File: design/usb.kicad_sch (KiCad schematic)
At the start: 27 parts, among them J4 USB_B_Mini, SW1 RST, U7 SN74LVC1G11DCKR, U8 USBLC6-2SC6, U9 FT231XS

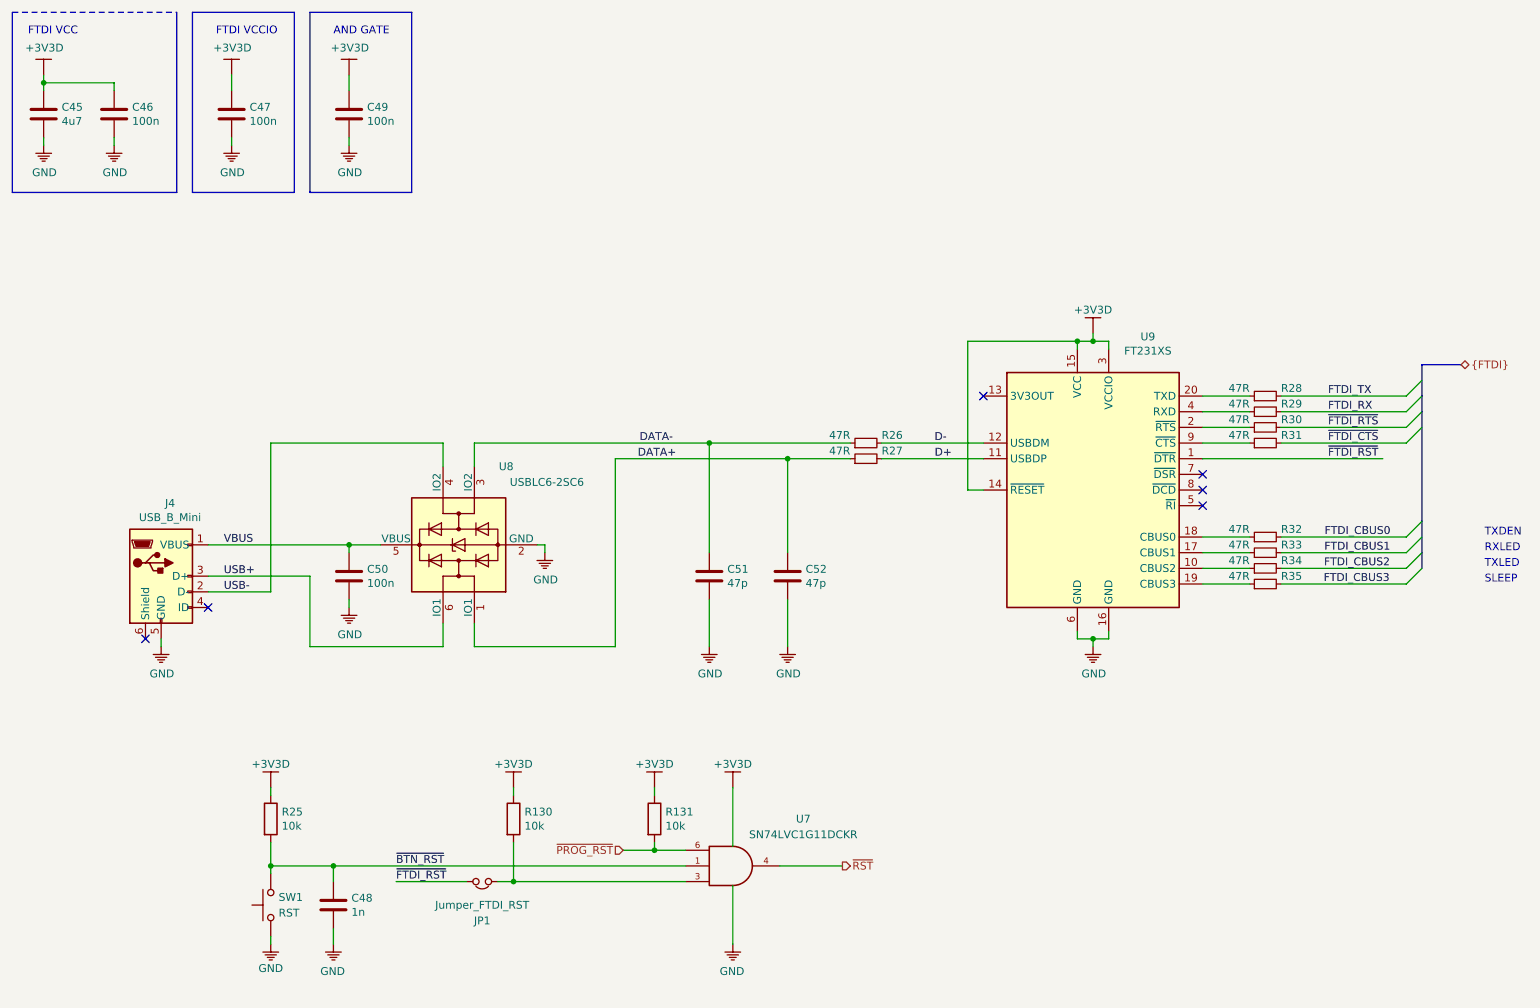
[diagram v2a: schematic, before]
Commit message: Added fiducials
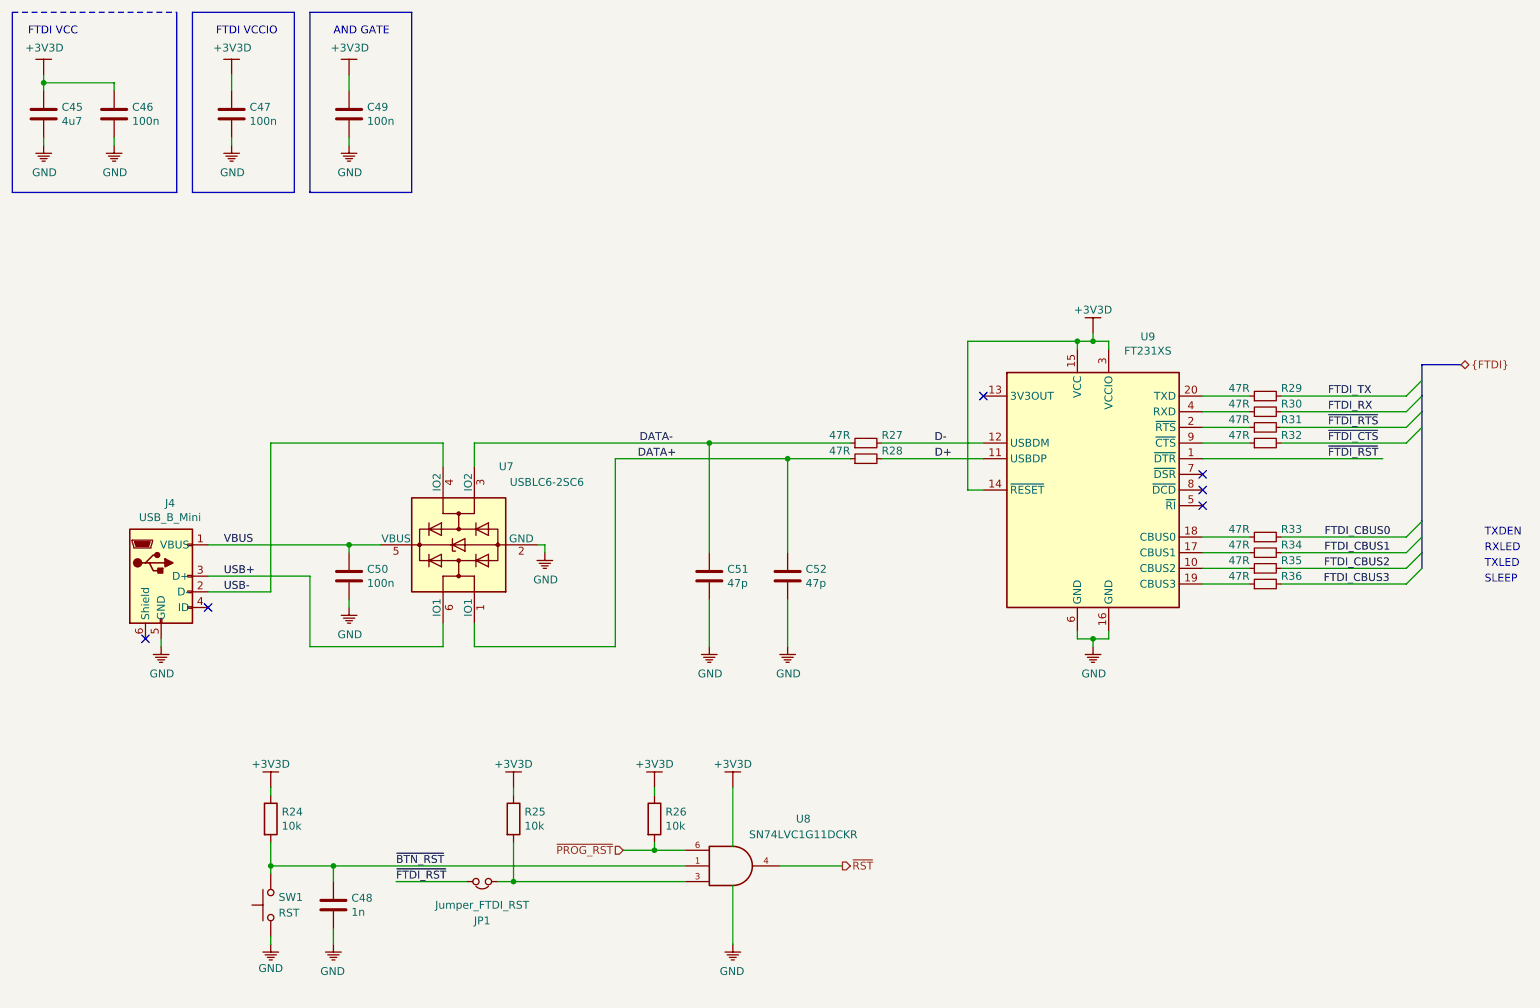
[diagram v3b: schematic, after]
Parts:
- renumbered R25 to R24, R130 to R25, R131 to R26, R26 to R27, R27 to R28, R28 to R29, R29 to R30, R30 to R31, R31 to R32, R32 to R33, R33 to R34, R34 to R35, R35 to R36, U8 to U7, U7 to U8
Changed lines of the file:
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@@
   )
   (symbol (lib_id "KLIB_Power:+3V3D") (at 20.32 25.4 0) (unit 1)
-    (property "Reference" "#PWR089" (id 0) (at 20.32 33.02 0)
+    (property "Reference" "#PWR090" (id 0) (at 20.32 33.02 0)
       (effects (font (size 1.27 1.27)) hide)
     )
@@
   )
   (symbol (lib_id "KLIB_Power:GND") (at 20.32 36.83 0) (unit 1)
-    (property "Reference" "#PWR090" (id 0) (at 20.32 41.91 0)
+    (property "Reference" "#PWR091" (id 0) (at 20.32 41.91 0)
       (effects (font (size 1.27 1.27)) hide)
     )
@@
   )
   (symbol (lib_id "KLIB_Power:GND") (at 31.75 36.83 0) (unit 1)
-    (property "Reference" "#PWR091" (id 0) (at 31.75 41.91 0)
+    (property "Reference" "#PWR092" (id 0) (at 31.75 41.91 0)
       (effects (font (size 1.27 1.27)) hide)
     )
@@
   )
   (symbol (lib_id "KLIB_Power:GND") (at 39.37 118.11 0) (unit 1)
-    (property "Reference" "#PWR092" (id 0) (at 39.37 123.19 0)
+    (property "Reference" "#PWR093" (id 0) (at 39.37 123.19 0)
       (effects (font (size 1.27 1.27)) hide)
     )
@@
   )
   (symbol (lib_id "KLIB_Power:+3V3D") (at 50.8 25.4 0) (unit 1)
-    (property "Reference" "#PWR095" (id 0) (at 50.8 33.02 0)
+    (property "Reference" "#PWR094" (id 0) (at 50.8 33.02 0)
       (effects (font (size 1.27 1.27)) hide)
     )
@@
   )
   (symbol (lib_id "KLIB_Power:GND") (at 50.8 36.83 0) (unit 1)
-    (property "Reference" "#PWR096" (id 0) (at 50.8 41.91 0)
+    (property "Reference" "#PWR095" (id 0) (at 50.8 41.91 0)
       (effects (font (size 1.27 1.27)) hide)
     )
@@
   )
   (symbol (lib_id "KLIB_Power:+3V3D") (at 57.15 140.97 0) (unit 1)
-    (property "Reference" "#PWR093" (id 0) (at 57.15 148.59 0)
+    (property "Reference" "#PWR096" (id 0) (at 57.15 148.59 0)
       (effects (font (size 1.27 1.27)) hide)
     )
@@
   )
   (symbol (lib_id "KLIB_Power:GND") (at 57.15 166.37 0) (unit 1)
-    (property "Reference" "#PWR094" (id 0) (at 57.15 171.45 0)
+    (property "Reference" "#PWR097" (id 0) (at 57.15 171.45 0)
       (effects (font (size 1.27 1.27)) hide)
     )
@@
   )
   (symbol (lib_id "KLIB_Power:GND") (at 67.31 166.37 0) (mirror y) (unit 1)
-    (property "Reference" "#PWR097" (id 0) (at 67.31 171.45 0)
+    (property "Reference" "#PWR098" (id 0) (at 67.31 171.45 0)
       (effects (font (size 1.27 1.27)) hide)
     )
@@
   )
   (symbol (lib_id "KLIB_Power:+3V3D") (at 69.85 25.4 0) (unit 1)
-    (property "Reference" "#PWR0221" (id 0) (at 69.85 33.02 0)
+    (property "Reference" "#PWR099" (id 0) (at 69.85 33.02 0)
       (effects (font (size 1.27 1.27)) hide)
     )
@@
   )
   (symbol (lib_id "KLIB_Power:GND") (at 69.85 36.83 0) (unit 1)
-    (property "Reference" "#PWR0220" (id 0) (at 69.85 41.91 0)
+    (property "Reference" "#PWR0100" (id 0) (at 69.85 41.91 0)
       (effects (font (size 1.27 1.27)) hide)
     )
@@
   )
   (symbol (lib_id "KLIB_Power:GND") (at 69.85 111.76 0) (unit 1)
-    (property "Reference" "#PWR0100" (id 0) (at 69.85 116.84 0)
+    (property "Reference" "#PWR0101" (id 0) (at 69.85 116.84 0)
       (effects (font (size 1.27 1.27)) hide)
     )
@@
   )
   (symbol (lib_id "KLIB_Power:+3V3D") (at 96.52 140.97 0) (unit 1)
-    (property "Reference" "#PWR098" (id 0) (at 96.52 148.59 0)
+    (property "Reference" "#PWR0102" (id 0) (at 96.52 148.59 0)
       (effects (font (size 1.27 1.27)) hide)
     )
@@
   )
   (symbol (lib_id "KLIB_Power:+3V3D") (at 119.38 140.97 0) (unit 1)
-    (property "Reference" "#PWR099" (id 0) (at 119.38 148.59 0)
+    (property "Reference" "#PWR0104" (id 0) (at 119.38 148.59 0)
       (effects (font (size 1.27 1.27)) hide)
     )
@@
   )
   (symbol (lib_id "KLIB_Power:GND") (at 128.27 118.11 0) (unit 1)
-    (property "Reference" "#PWR0104" (id 0) (at 128.27 123.19 0)
+    (property "Reference" "#PWR0105" (id 0) (at 128.27 123.19 0)
       (effects (font (size 1.27 1.27)) hide)
     )
@@
   )
   (symbol (lib_id "KLIB_Power:+3V3D") (at 132.08 140.97 0) (unit 1)
-    (property "Reference" "#PWR0101" (id 0) (at 132.08 148.59 0)
+    (property "Reference" "#PWR0106" (id 0) (at 132.08 148.59 0)
       (effects (font (size 1.27 1.27)) hide)
     )
@@
   )
   (symbol (lib_id "KLIB_Power:GND") (at 132.08 166.37 0) (mirror y) (unit 1)
-    (property "Reference" "#PWR0102" (id 0) (at 132.08 171.45 0)
+    (property "Reference" "#PWR0107" (id 0) (at 132.08 171.45 0)
       (effects (font (size 1.27 1.27)) hide)
     )
@@
   )
   (symbol (lib_id "KLIB_Power:GND") (at 140.97 118.11 0) (unit 1)
-    (property "Reference" "#PWR0105" (id 0) (at 140.97 123.19 0)
+    (property "Reference" "#PWR0108" (id 0) (at 140.97 123.19 0)
       (effects (font (size 1.27 1.27)) hide)
     )
@@
   )
   (symbol (lib_id "KLIB_Power:+3V3D") (at 190.5 67.31 0) (unit 1)
-    (property "Reference" "#PWR0106" (id 0) (at 190.5 74.93 0)
+    (property "Reference" "#PWR0109" (id 0) (at 190.5 74.93 0)
       (effects (font (size 1.27 1.27)) hide)
     )
@@
   )
   (symbol (lib_id "KLIB_Power:GND") (at 190.5 118.11 0) (unit 1)
-    (property "Reference" "#PWR0107" (id 0) (at 190.5 123.19 0)
+    (property "Reference" "#PWR0110" (id 0) (at 190.5 123.19 0)
       (effects (font (size 1.27 1.27)) hide)
     )
@@
   )
   (symbol (lib_id "Device:R_Small") (at 153.67 85.09 90) (unit 1)
-    (property "Reference" "R26" (id 0) (at 156.21 83.82 90)
+    (property "Reference" "R27" (id 0) (at 156.21 83.82 90)
       (effects (font (size 1.27 1.27)) (justify right))
     )
@@
   )
   (symbol (lib_id "Device:R_Small") (at 153.67 87.63 90) (unit 1)
-    (property "Reference" "R27" (id 0) (at 156.21 86.36 90)
+    (property "Reference" "R28" (id 0) (at 156.21 86.36 90)
       (effects (font (size 1.27 1.27)) (justify right))
     )
@@
   )
   (symbol (lib_id "Device:R_Small") (at 218.44 77.47 90) (unit 1)
-    (property "Reference" "R28" (id 0) (at 220.98 76.2 90)
+    (property "Reference" "R29" (id 0) (at 220.98 76.2 90)
       (effects (font (size 1.27 1.27)) (justify right))
     )
@@
   )
   (symbol (lib_id "Device:R_Small") (at 218.44 80.01 90) (unit 1)
-    (property "Reference" "R29" (id 0) (at 220.98 78.74 90)
+    (property "Reference" "R30" (id 0) (at 220.98 78.74 90)
       (effects (font (size 1.27 1.27)) (justify right))
     )
@@
   )
   (symbol (lib_id "Device:R_Small") (at 218.44 82.55 90) (unit 1)
-    (property "Reference" "R30" (id 0) (at 220.98 81.28 90)
+    (property "Reference" "R31" (id 0) (at 220.98 81.28 90)
       (effects (font (size 1.27 1.27)) (justify right))
     )
@@
   )
   (symbol (lib_id "Device:R_Small") (at 218.44 85.09 90) (unit 1)
-    (property "Reference" "R31" (id 0) (at 220.98 83.82 90)
+    (property "Reference" "R32" (id 0) (at 220.98 83.82 90)
       (effects (font (size 1.27 1.27)) (justify right))
     )
@@
   )
   (symbol (lib_id "Device:R_Small") (at 218.44 100.33 90) (unit 1)
-    (property "Reference" "R32" (id 0) (at 220.98 99.06 90)
+    (property "Reference" "R33" (id 0) (at 220.98 99.06 90)
       (effects (font (size 1.27 1.27)) (justify right))
     )
@@
   )
   (symbol (lib_id "Device:R_Small") (at 218.44 102.87 90) (unit 1)
-    (property "Reference" "R33" (id 0) (at 220.98 101.6 90)
+    (property "Reference" "R34" (id 0) (at 220.98 101.6 90)
       (effects (font (size 1.27 1.27)) (justify right))
     )
@@
   )
   (symbol (lib_id "Device:R_Small") (at 218.44 105.41 90) (unit 1)
-    (property "Reference" "R34" (id 0) (at 220.98 104.14 90)
+    (property "Reference" "R35" (id 0) (at 220.98 104.14 90)
       (effects (font (size 1.27 1.27)) (justify right))
     )
@@
   )
   (symbol (lib_id "Device:R_Small") (at 218.44 107.95 90) (unit 1)
-    (property "Reference" "R35" (id 0) (at 220.98 106.68 90)
+    (property "Reference" "R36" (id 0) (at 220.98 106.68 90)
       (effects (font (size 1.27 1.27)) (justify right))
     )
@@
   )
   (symbol (lib_id "Device:R") (at 57.15 146.05 0) (unit 1)
-    (property "Reference" "R25" (id 0) (at 58.928 144.907 0)
+    (property "Reference" "R24" (id 0) (at 58.928 144.907 0)
       (effects (font (size 1.27 1.27)) (justify left))
     )
@@
   )
   (symbol (lib_id "Device:R") (at 96.52 146.05 0) (unit 1)
-    (property "Reference" "R130" (id 0) (at 98.298 144.907 0)
+    (property "Reference" "R25" (id 0) (at 98.298 144.907 0)
       (effects (font (size 1.27 1.27)) (justify left))
     )
@@
   )
   (symbol (lib_id "Device:R") (at 119.38 146.05 0) (unit 1)
-    (property "Reference" "R131" (id 0) (at 121.158 144.907 0)
+    (property "Reference" "R26" (id 0) (at 121.158 144.907 0)
       (effects (font (size 1.27 1.27)) (justify left))
     )
@@
   )
   (symbol (lib_id "74xGxx:74LVC1G11") (at 132.08 153.67 0) (unit 1)
-    (property "Reference" "U7" (id 0) (at 143.51 146.05 0))
+    (property "Reference" "U8" (id 0) (at 143.51 146.05 0))
     (property "Value" "SN74LVC1G11DCKR" (id 1) (at 143.51 148.59 0))
     (property "Footprint" "Package_TO_SOT_SMD:SOT-363_SC-70-6" (id 2) (at 132.08 153.67 0)
@@
   )
   (symbol (lib_id "digitizer_fpga_10b_100MSPS-rescue:USBLC6-2SC6-Power_Protection") (at 87.63 101.6 90) (unit 1)
-    (property "Reference" "U8" (id 0) (at 96.52 88.9 90)
-      (effects (font (size 1.27 1.27)) (justify left))
-    )
+    (property "Reference" "U7" (id 0) (at 96.52 88.9 90)
+      (effects (font (size 1.27 1.27)) (justify left))
+    )

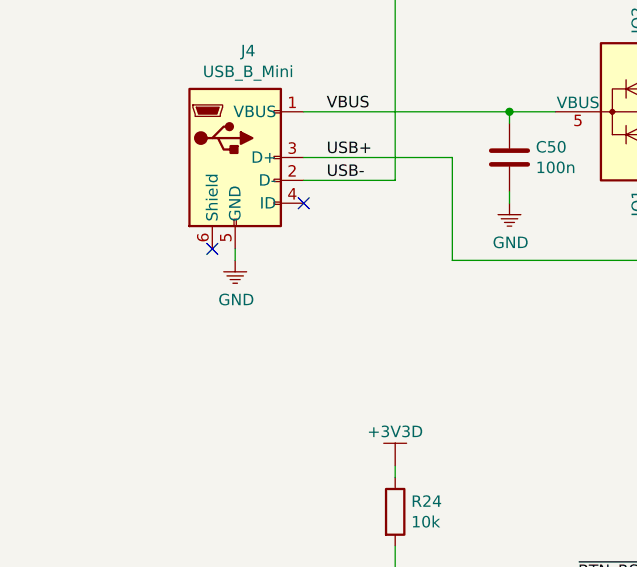
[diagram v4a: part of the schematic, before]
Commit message: Connected USB shield to GND
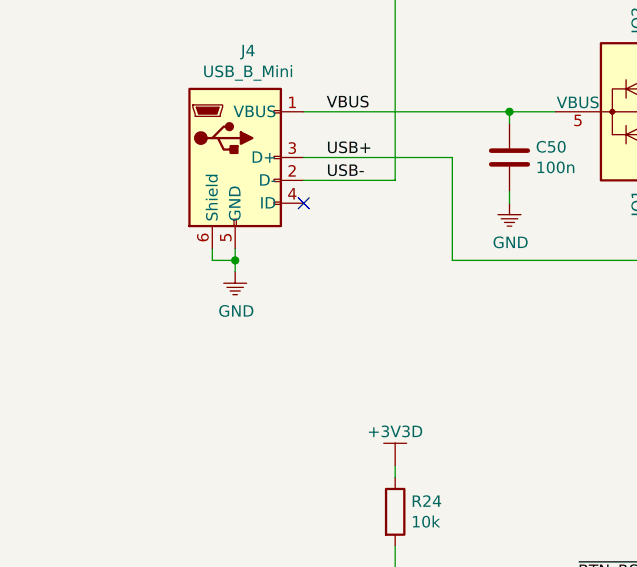
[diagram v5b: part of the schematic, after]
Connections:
- net GND: now also J4.6 (Shield)
- no-connect marks 6 -> 5
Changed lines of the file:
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@@
   (bus_alias "FTDI" (members "FTDI_TX" "FTDI_RX" "~FTDI_RTS" "~FTDI_CTS" "FTDI_CBUS[0..3]"))
   (junction (at 20.32 26.67))
+  (junction (at 39.37 118.11))
   (junction (at 57.15 153.67))
   (junction (at 67.31 153.67))
@@
   (no_connect (at 208.28 92.71))
   (no_connect (at 46.99 111.76))
-  (no_connect (at 36.83 116.84))
   (no_connect (at 208.28 90.17))
   (bus_entry (at 241.3 77.47) (size 2.54 -2.54))
@@
   (wire (pts (xy 31.75 26.67) (xy 31.75 27.94)))
   (wire (pts (xy 31.75 35.56) (xy 31.75 36.83)))
+  (wire (pts (xy 36.83 116.84) (xy 36.83 118.11)))
+  (wire (pts (xy 36.83 118.11) (xy 39.37 118.11)))
   (wire (pts (xy 39.37 116.84) (xy 39.37 118.11)))
+  (wire (pts (xy 39.37 118.11) (xy 39.37 119.38)))
   (wire (pts (xy 46.99 101.6) (xy 69.85 101.6)))
   (wire (pts (xy 46.99 106.68) (xy 63.5 106.68)))
@@
     )
   )
-  (symbol (lib_id "KLIB_Power:GND") (at 39.37 118.11 0) (unit 1)
-    (property "Reference" "#PWR093" (id 0) (at 39.37 123.19 0)
-      (effects (font (size 1.27 1.27)) hide)
-    )
-    (property "Value" "GND" (id 1) (at 39.497 122.5042 0))
-    (property "Footprint" "" (id 2) (at 39.37 118.11 0)
-      (effects (font (size 1.27 1.27)) hide)
-    )
-    (property "Datasheet" "" (id 3) (at 39.37 118.11 0)
-      (effects (font (size 1.27 1.27)) hide)
-    )
+  (symbol (lib_id "KLIB_Power:GND") (at 39.37 119.38 0) (unit 1)
+    (property "Reference" "#PWR093" (id 0) (at 39.37 124.46 0)
+      (effects (font (size 1.27 1.27)) hide)
+    )
+    (property "Value" "GND" (id 1) (at 39.497 123.7742 0))
+    (property "Footprint" "" (id 2) (at 39.37 119.38 0)
+      (effects (font (size 1.27 1.27)) hide)
+    )
+    (property "Datasheet" "" (id 3) (at 39.37 119.38 0)
+      (effects (font (size 1.27 1.27)) hide)
+    )

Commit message: Updated LNA
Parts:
- R24, R25, R26: value 10k -> 4k7
